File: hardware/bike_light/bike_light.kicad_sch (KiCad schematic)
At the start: 48 parts, among them J1 Battery, J2 USB_C_Receptacle_USB2.0_16P, SW1 SW_Push, SW2 SW_Push, U1 TPS22918DBV, U2 ESP32-C3-WROOM-02, U3 XC6220B331MR, U4 BQ21040DBV

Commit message: PCB updates
* Added USB step file
* Added side push button step file
* Moved debug pads for cleaner layout
* Added some silkscreening with model name/version.
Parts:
- added TP1: 3V3, TestPoint:TestPoint_Pad_D1.0mm, symbol Connector:TestPoint
- added TP2: EN, TestPoint:TestPoint_Pad_D1.0mm, symbol Connector:TestPoint
- added TP3: IO9_BOOT, TestPoint:TestPoint_Pad_D1.0mm, symbol Connector:TestPoint
- added TP4: TXD, TestPoint:TestPoint_Pad_D1.0mm, symbol Connector:TestPoint
- added TP5: RXD, TestPoint:TestPoint_Pad_D1.0mm, symbol Connector:TestPoint
- added TP6: GND, TestPoint:TestPoint_Pad_D1.0mm, symbol Connector:TestPoint
- J2: footprint Connector_USB:USB_C_Receptacle_HRO_TYPE-C-31-M-12 -> bike_light:USB_C_Receptacle_HRO_TYPE-C-31-M-12
- SW1: footprint Button_Switch_SMD:SW_Push_1P1T-MP_NO_Horizontal_Alps_SKRTLAE010 -> bike_light:SW_Push_1P1T-MP_NO_Horizontal_Alps_SKRTLAE010
- U2: footprint bike_light:ESP32-C3-WROOM-02_NoVias -> RF_Module:ESP32-C3-WROOM-02
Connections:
- net +3.3V: now also TP1.1
- net ESP_EN: now also TP2.1
- net GND: now also TP6.1
- net UART_RX: now reaches U2.11 (IO20/RXD)
- net UART_RX: now also TP5.1
- net UART_TX: now reaches U2.12 (IO21/TXD)
- net UART_TX: now also TP4.1
- net BOOT: now reaches SW2.2, U2.8 (IO9)
- net BOOT: now also TP3.1
- no-connect marks 8 -> 6
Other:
- note added: "Recovery Test Pads"

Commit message: Updated PCB and new models
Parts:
- U2: footprint RF_Module:ESP32-C3-WROOM-02 -> bike_light:ESP32-C3-WROOM-02_NoVias
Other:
- title: (none) -> gladish_bl
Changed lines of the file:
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@@
 	(generator_version "10.0")
 	(paper "A3")
+	(title_block
+		(title "gladish_bl")
+		(date "2026-10-16")
+		(rev "0.0.1")
+	)
 	(rectangle
 		(start 24.13 196.85)
@@
 			)
 		)
-		(property "Footprint" "RF_Module:ESP32-C3-WROOM-02"
+		(property "Footprint" "bike_light:ESP32-C3-WROOM-02_NoVias"
 			(at 91.44 231.775 0)
 			(hide yes)

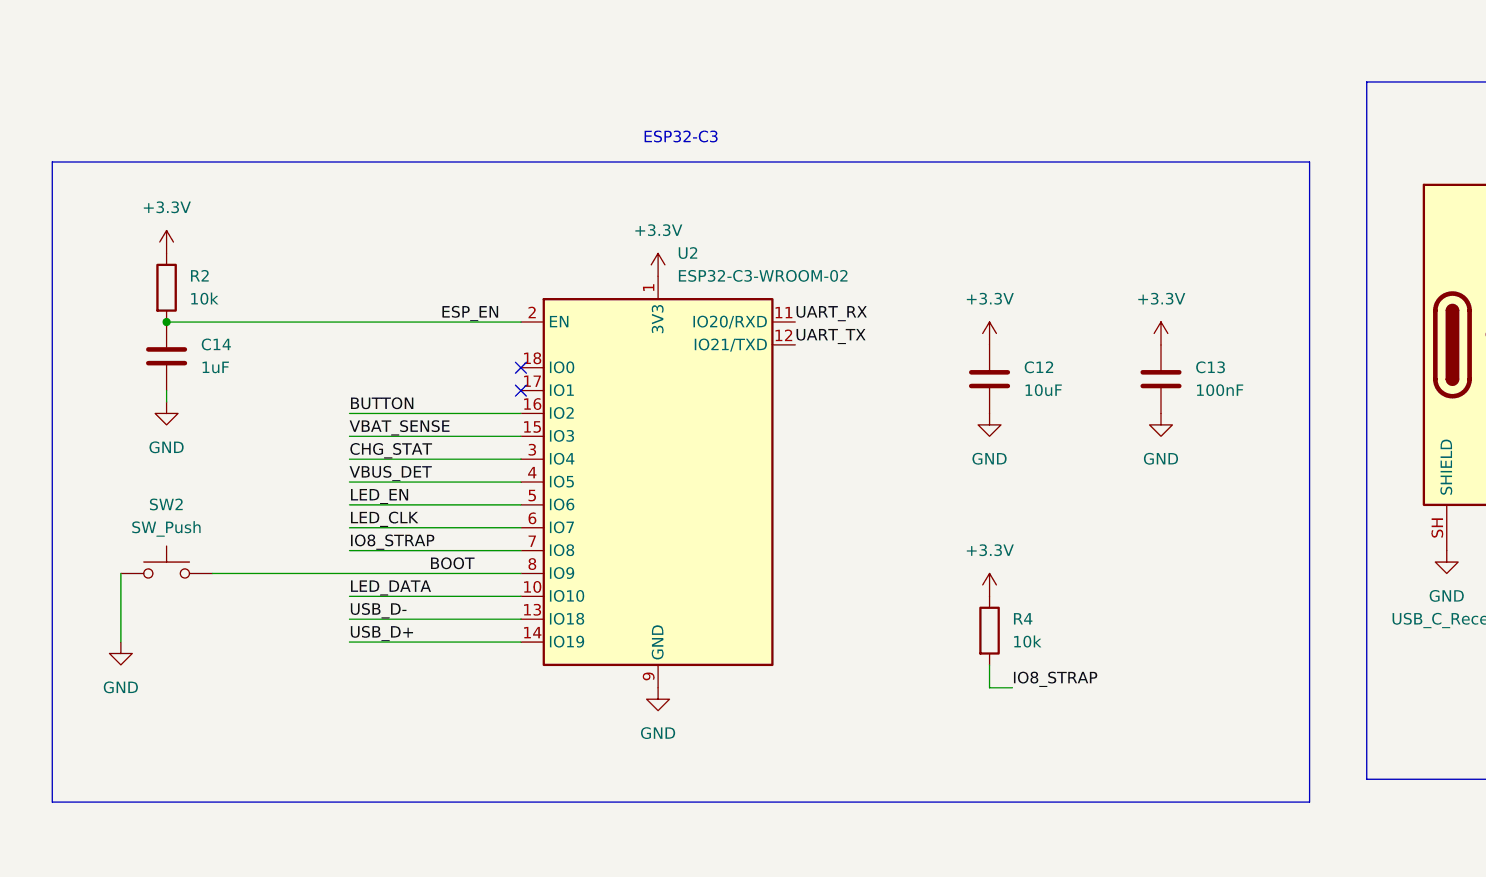
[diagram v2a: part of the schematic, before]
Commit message: Switched to ESP32-C3-MINI-1, shrunk board
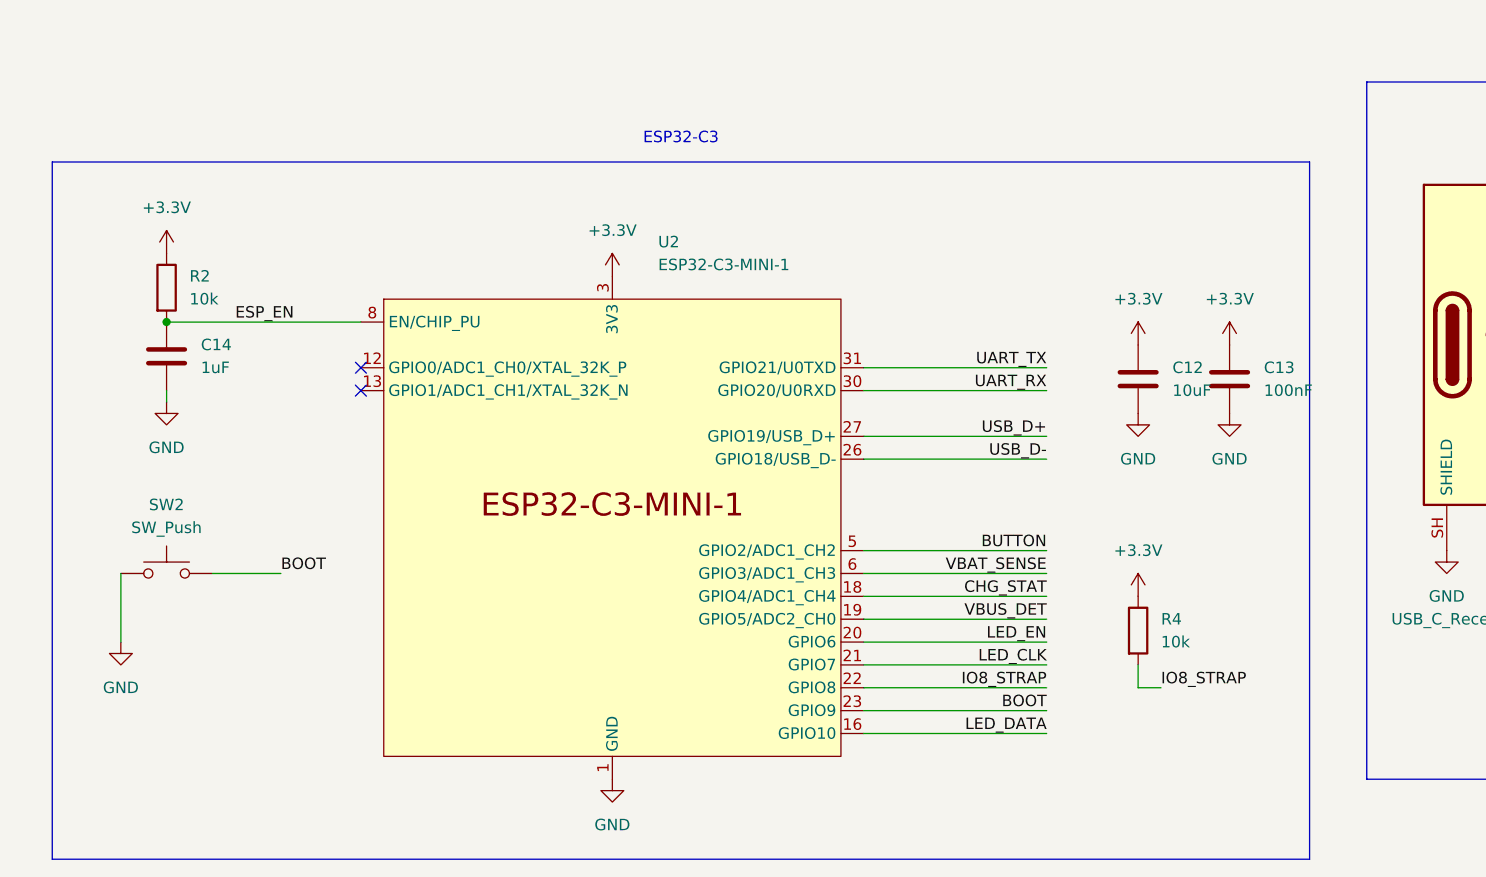
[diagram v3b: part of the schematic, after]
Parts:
- U2: value ESP32-C3-WROOM-02 -> ESP32-C3-MINI-1; footprint bike_light:ESP32-C3-WROOM-02_NoVias -> bike_light:ESP32-C3-MINI-1; symbol RF_Module:ESP32-C3-WROOM-02 -> bike_light:ESP32-C3-MINI-1
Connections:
- net +3.3V: now also U2.3 (3V3); no longer U2.1 (3V3)
- net BOOT: now also U2.23 (GPIO9); no longer U2.8 (IO9)
- net BUTTON: now also U2.5 (GPIO2/ADC1_CH2); no longer U2.16 (IO2)
- net CHG_STAT: now also U2.18 (GPIO4/ADC1_CH4); no longer U2.3 (IO4)
- net ESP_EN: now also U2.8 (EN/CHIP_PU); no longer U2.2 (EN)
- net GND: now also U2.1 (GND), U2.11 (GND), U2.14 (GND), U2.2 (GND), U2.36 (GND), U2.37 (GND), U2.38 (GND), U2.39 (GND), U2.40 (GND), U2.41 (GND), U2.42 (GND), U2.43 (GND), U2.44 (GND), U2.45 (GND), U2.46 (GND), U2.47 (GND), U2.48 (GND), U2.49 (GND), U2.50 (GND), U2.51 (GND), U2.52 (GND), U2.53 (GND); no longer U2.19 (GND), U2.9 (GND)
- net IO8_STRAP: now also U2.22 (GPIO8); no longer U2.7 (IO8)
- net LED_CLK: now also U2.21 (GPIO7); no longer U2.6 (IO7)
- net LED_DATA: now also U2.16 (GPIO10); no longer U2.10 (IO10)
- net LED_EN: now also U2.20 (GPIO6); no longer U2.5 (IO6)
- net UART_RX: now also U2.30 (GPIO20/U0RXD); no longer U2.11 (IO20/RXD)
- net UART_TX: now also U2.31 (GPIO21/U0TXD); no longer U2.12 (IO21/TXD)
- net USB_D+: now also U2.27 (GPIO19/USB_D+); no longer U2.14 (IO19)
- net USB_D-: now also U2.26 (GPIO18/USB_D-); no longer U2.13 (IO18)
- net VBAT_SENSE: now also U2.6 (GPIO3/ADC1_CH3); no longer U2.15 (IO3)
- net VBUS_DET: now also U2.19 (GPIO5/ADC2_CH0); no longer U2.4 (IO5)
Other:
- moved on the sheet: C12, C13, R4
